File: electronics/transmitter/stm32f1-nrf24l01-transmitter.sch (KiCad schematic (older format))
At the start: 29 parts, among them K1 CONN_3, K10 CONN_3, K11 CONN_3, K2 CONN_3, K3 CONN_3, K4 CONN_3, K5 CONN_3, K6 CONN_3, K7 CONN_3, K8 CONN_3, K9 CONN_3, P1 Charge, P2 LED, P3 CONN_2, P4 CONN_2, P5 CONN_4, Q1 BC548, SW1 ON/OFF, U1 LIPO_CHARGER_+_PROTECTION, U2 STM32F103C8T6_DEV_BOARD, U3 NRF24L01P

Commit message: Update schematics
- Convert to KiCAD 4.05
- Dummy links accross battery connector for routing purpos
- Dummy connector for speaker
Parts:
- removed P5: CONN_4, symbol CONN_4
- added K12: CONN_3, Pin_Headers:Pin_Header_Straight_1x03_Pitch2.54mm, symbol CONN_3
- added P5: Buzzer, Pin_Headers:Pin_Header_Straight_1x02_Pitch2.54mm, symbol CONN_2
- BT1: footprint ~ -> (none)
- C1, C2: footprint ~ -> Capacitors_SMD:C_0805_HandSoldering; symbol C -> C-RESCUE-stm32f1-nrf24l01-transmitter
- K1, K10, K11, K2, K3, K4, K5, K6, K7, K8, K9: footprint (none) -> Pin_Headers:Pin_Header_Straight_1x03_Pitch2.54mm
- P1, P2, P3, P4: footprint (none) -> Pin_Headers:Pin_Header_Straight_1x02_Pitch2.54mm
- Q1: footprint ~ -> TO_SOT_Packages_THT:TO-92_Molded_Wide
- R1, R2, R3, R4: footprint ~ -> Resistors_SMD:R_0805_HandSoldering; symbol R -> R-RESCUE-stm32f1-nrf24l01-transmitter
- SP1: footprint ~ -> Buzzers_Beepers:Buzzer_12x9.5RM7.6
- SW1: footprint ~ -> Buttons_Switches_SMD:SW_SPST_FSMSM
- U1: footprint ~ -> WLA:LiPo_charger_and_protection
- U2: footprint ~ -> WLA:STM32F103C8T6
- U3: footprint ~ -> WLA:NRF24L01P-PA-LNA
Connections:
- wire segments 127 -> 131
- no-connect marks 5 -> 12
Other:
- note added: "Diagnostics UART"
- note removed: "Bluetooth SPP module\nDiagnostics UART"
- moved on the sheet: C1, C2, P2, Q1, SP1, U2, U3

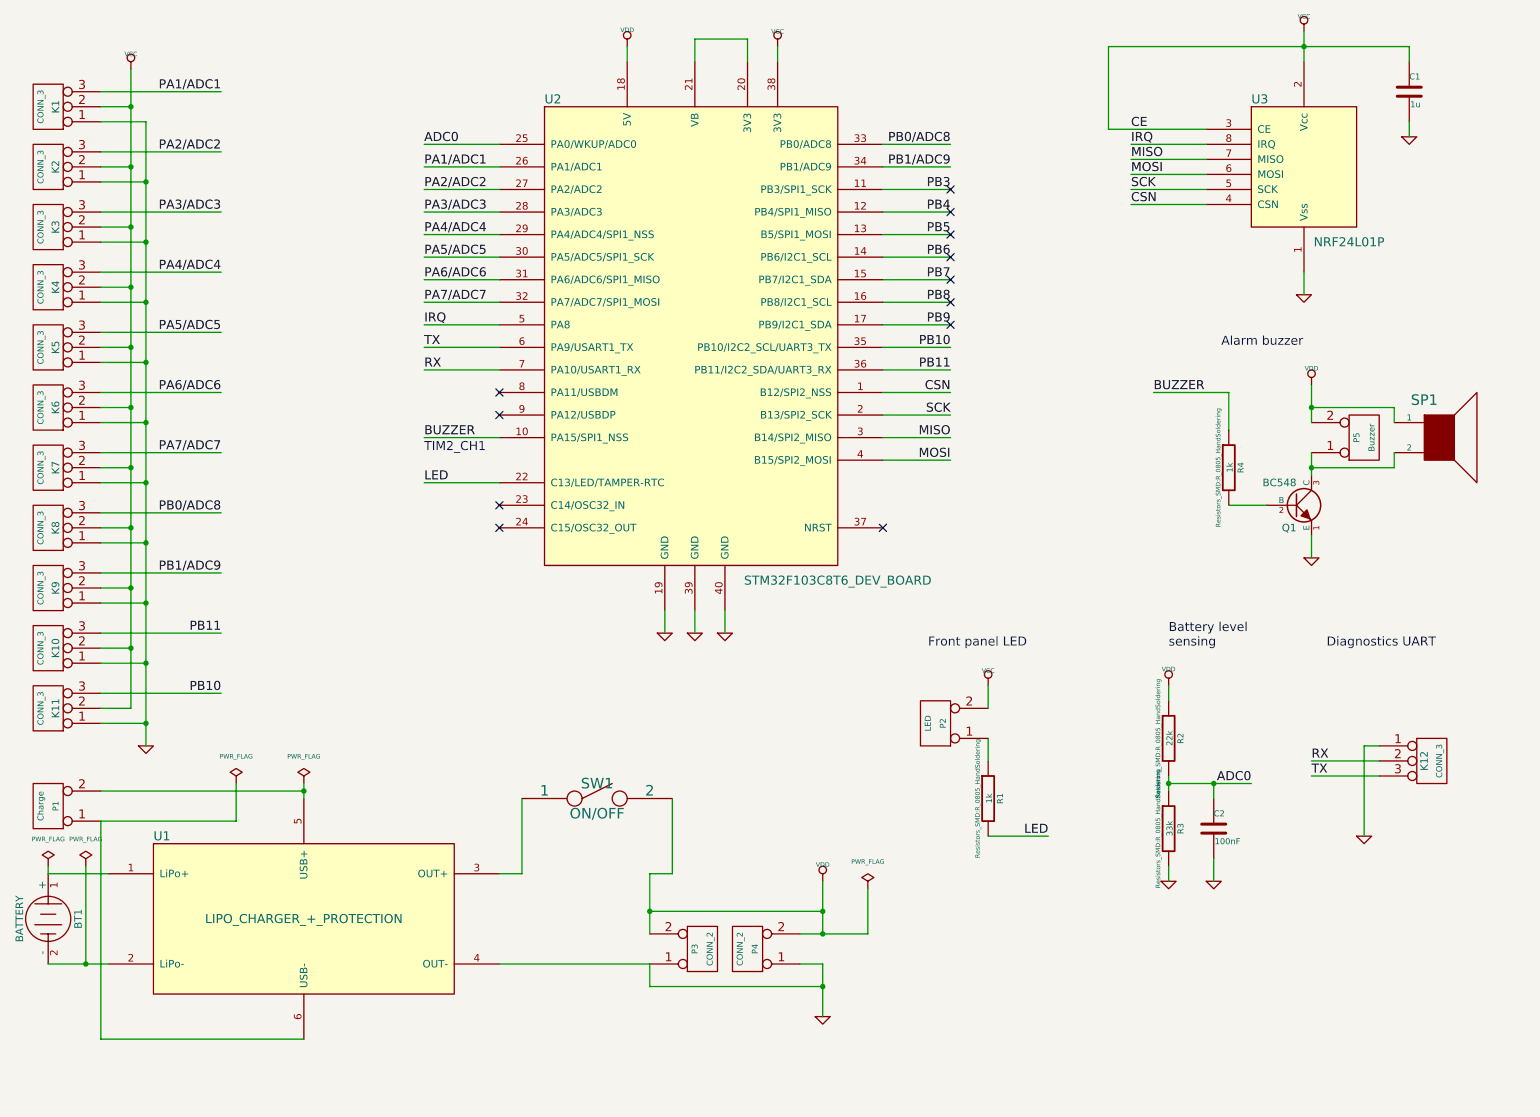
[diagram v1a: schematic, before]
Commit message: Tweak design to reduce space and wire links
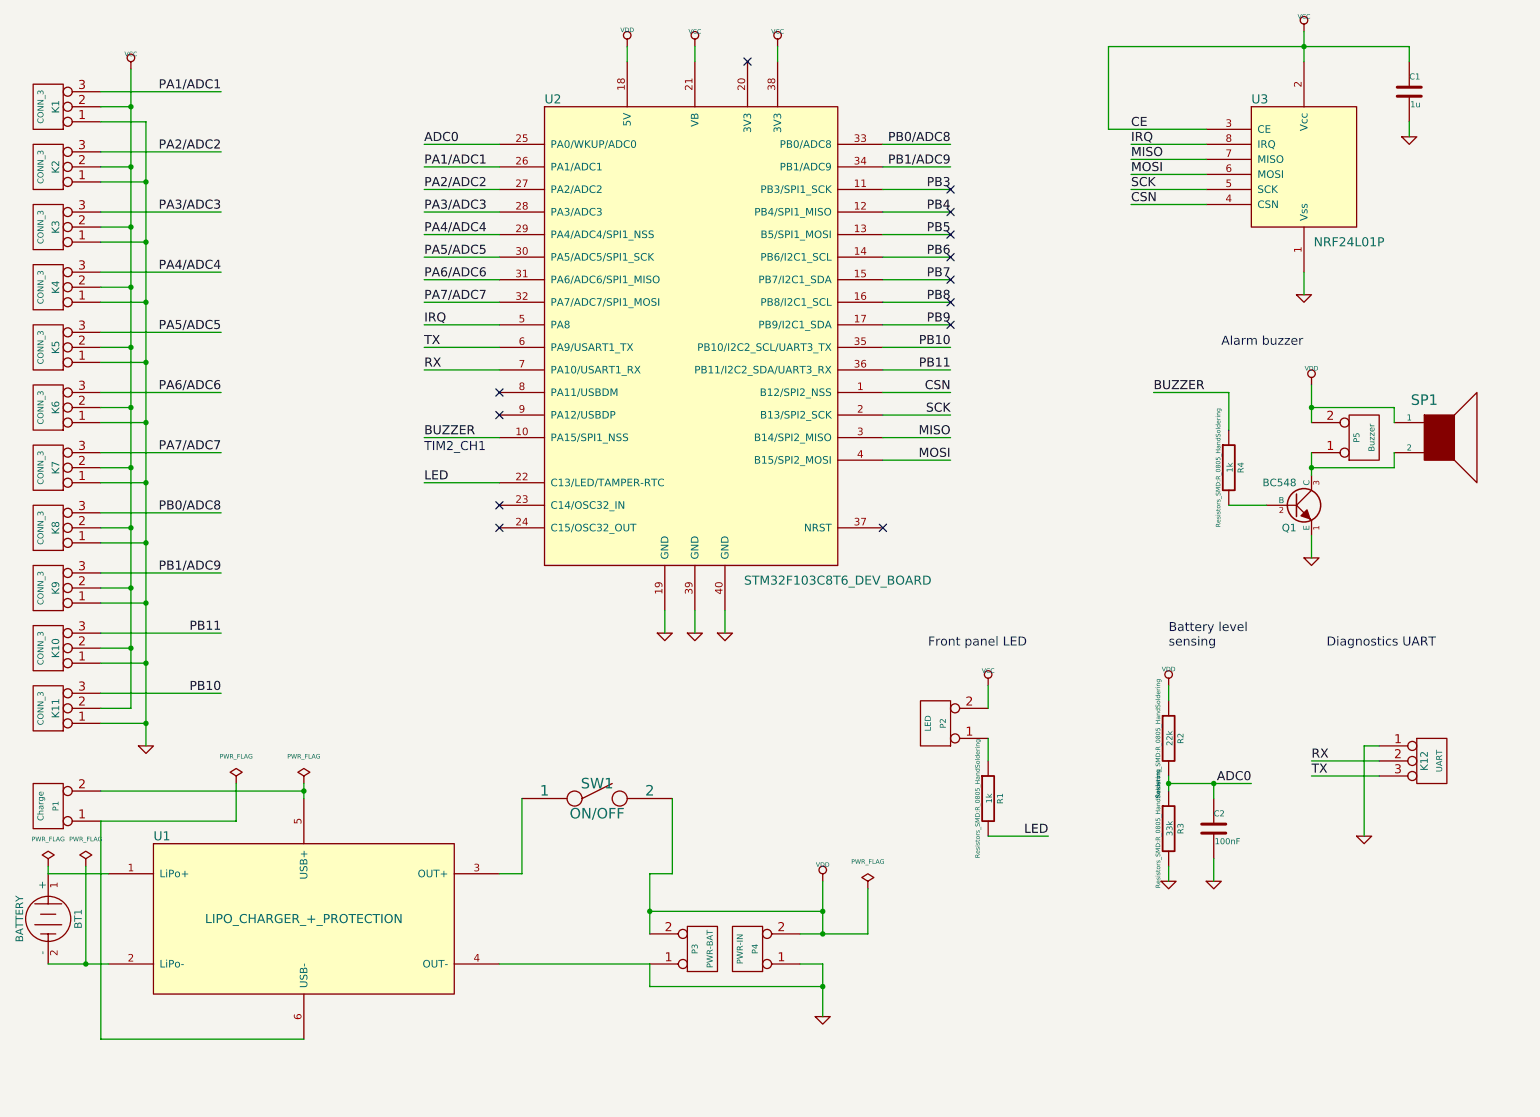
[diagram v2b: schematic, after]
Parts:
- K12: value CONN_3 -> UART
- P3: value CONN_2 -> PWR-BAT
- P4: value CONN_2 -> PWR-IN
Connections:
- net VCC: now also U2.21 (VB)
- net at U2.20 (3V3): no longer U2.21 (VB)
- no-connect marks 12 -> 13
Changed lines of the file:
@@
 P 5950 6850
 F 0 "P4" V 5900 6850 40  0000 C CNN
-F 1 "CONN_2" V 6000 6850 40  0000 C CNN
+F 1 "PWR-IN" V 6000 6850 40  0000 C CNN
 F 2 "Pin_Headers:Pin_Header_Straight_1x02_Pitch2.54mm" H 5950 6850 60  0001 C CNN
 F 3 "" H 5950 6850 60  0000 C CNN
@@
 P 5650 6850
 F 0 "P3" V 5600 6850 40  0000 C CNN
-F 1 "CONN_2" V 5700 6850 40  0000 C CNN
+F 1 "PWR-BAT" V 5700 6850 40  0000 C CNN
 F 2 "Pin_Headers:Pin_Header_Straight_1x02_Pitch2.54mm" H 5650 6850 60  0001 C CNN
 F 3 "" H 5650 6850 60  0000 C CNN
@@
 P 10500 5600
 F 0 "K12" V 10450 5600 50  0000 C CNN
-F 1 "CONN_3" V 10550 5600 40  0000 C CNN
+F 1 "UART" V 10550 5600 40  0000 C CNN
 F 2 "Pin_Headers:Pin_Header_Straight_1x03_Pitch2.54mm" H 10500 5600 60  0001 C CNN
 F 3 "" H 10500 5600 60  0000 C CNN
@@
 Wire Wire Line
 	6150 850  6150 950
-Wire Wire Line
-	5600 950  5600 800
-Wire Wire Line
-	5600 800  5950 800
-Wire Wire Line
-	5950 800  5950 950
 Wire Wire Line
 	8350 850  10350 850
@@
 NoConn ~ 7300 2550
 NoConn ~ 7300 2700
+$Comp
+L VCC #PWR?
+U 1 1 589BC63C
+P 5600 850
+F 0 "#PWR?" H 5600 950 30  0001 C CNN
+F 1 "VCC" H 5600 950 30  0000 C CNN
+F 2 "" H 5600 850 60  0000 C CNN
+F 3 "" H 5600 850 60  0000 C CNN
+	1    5600 850
+	1    0    0    -1
+$EndComp
+Wire Wire Line
+	5600 850  5600 950
+NoConn ~ 5950 950
 $EndSCHEMATC

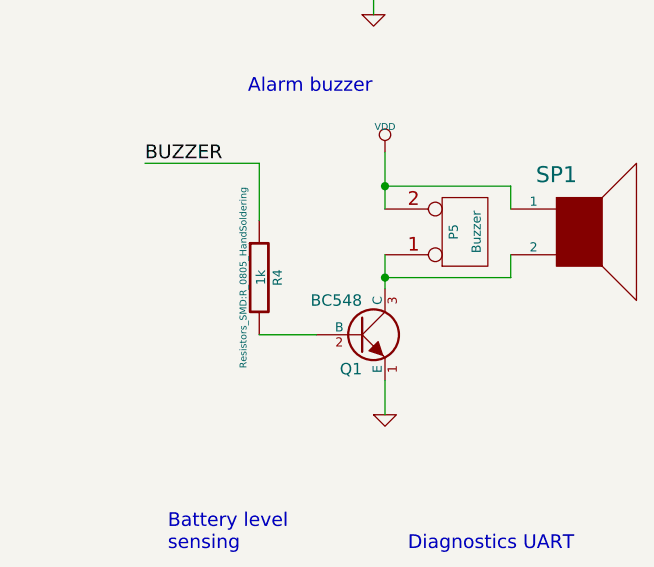
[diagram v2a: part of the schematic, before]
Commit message: Fix transistor footprint, add decoupling cap for buzzer, minor tweaks
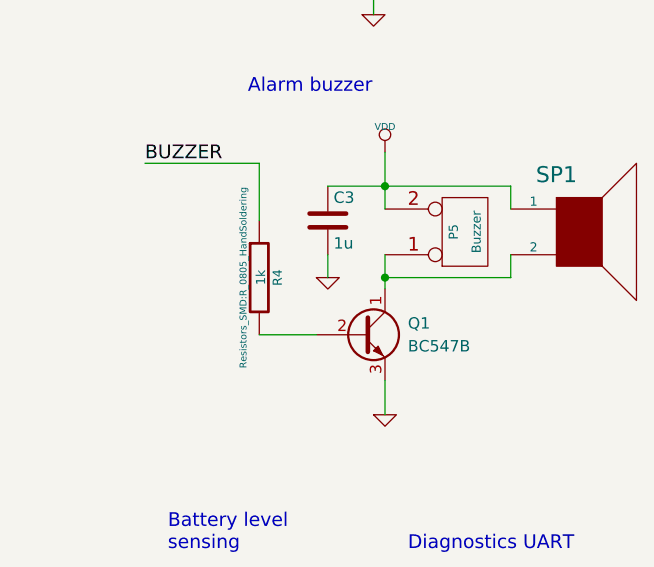
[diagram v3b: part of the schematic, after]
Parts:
- removed Q1: BC548, TO_SOT_Packages_THT:TO-92_Molded_Wide, symbol NPN
- added C3: 1u, Capacitors_SMD:C_0805_HandSoldering, symbol C
- added Q1: BC547B, TO_SOT_Packages_THT:TO-92_Inline_Wide, symbol Q_NPN_CBE
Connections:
- net GND: now also C3.2, Q1.3 (E)
- net VDD: now also C3.1
- net at P5.1 (P1), SP1.2: now also Q1.1 (C)
- net at R4.2: now also Q1.2 (B)
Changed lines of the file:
@@
-$EndComp
-$Comp
-L NPN Q1
-U 1 1 5720519E
-P 9600 3900
-F 0 "Q1" H 9600 3750 50  0000 R CNN
-F 1 "BC548" H 9600 4050 50  0000 R CNN
-F 2 "TO_SOT_Packages_THT:TO-92_Molded_Wide" H 9600 3900 60  0001 C CNN
-F 3 "~" H 9600 3900 60  0000 C CNN
-	1    9600 3900
-	1    0    0    -1
 $EndComp
 $Comp
@@
 Connection ~ 6450 7100
 Wire Wire Line
-	9700 3250 10250 3250
+	9450 3250 10250 3250
 Wire Wire Line
 	10250 3250 10250 3350
@@
 NoConn ~ 7300 2700
 $Comp
-L VCC #PWR?
+L VCC #PWR025
 U 1 1 589BC63C
 P 5600 850
-F 0 "#PWR?" H 5600 950 30  0001 C CNN
+F 0 "#PWR025" H 5600 950 30  0001 C CNN
 F 1 "VCC" H 5600 950 30  0000 C CNN
 F 2 "" H 5600 850 60  0000 C CNN
@@
 	5600 850  5600 950
 NoConn ~ 5950 950
+$Comp
+L Q_NPN_CBE Q1
+U 1 1 589EC521
+P 9600 3900
+F 0 "Q1" H 9800 3950 50  0000 L CNN
+F 1 "BC547B" H 9800 3850 50  0000 L CNN
+F 2 "TO_SOT_Packages_THT:TO-92_Inline_Wide" H 9800 4000 50  0001 C CNN
+F 3 "" H 9600 3900 50  0000 C CNN
+	1    9600 3900
+	1    0    0    -1
+$EndComp
+$Comp
+L C C3
+U 1 1 589ECC74
+P 9450 3400
+F 0 "C3" H 9475 3500 50  0000 L CNN
+F 1 "1u" H 9475 3300 50  0000 L CNN
+F 2 "Capacitors_SMD:C_0805_HandSoldering" H 9488 3250 50  0001 C CNN
+F 3 "" H 9450 3400 50  0000 C CNN
+	1    9450 3400
+	1    0    0    -1
+$EndComp
+$Comp
+L GND-RESCUE-stm32f1-nrf24l01-transmitter #PWR026
+U 1 1 589ECD1A
+P 9450 3650
+F 0 "#PWR026" H 9450 3650 30  0001 C CNN
+F 1 "GND" H 9450 3580 30  0001 C CNN
+F 2 "" H 9450 3650 60  0000 C CNN
+F 3 "" H 9450 3650 60  0000 C CNN
+	1    9450 3650
+	1    0    0    -1
+$EndComp
+Wire Wire Line
+	9450 3550 9450 3650
 $EndSCHEMATC

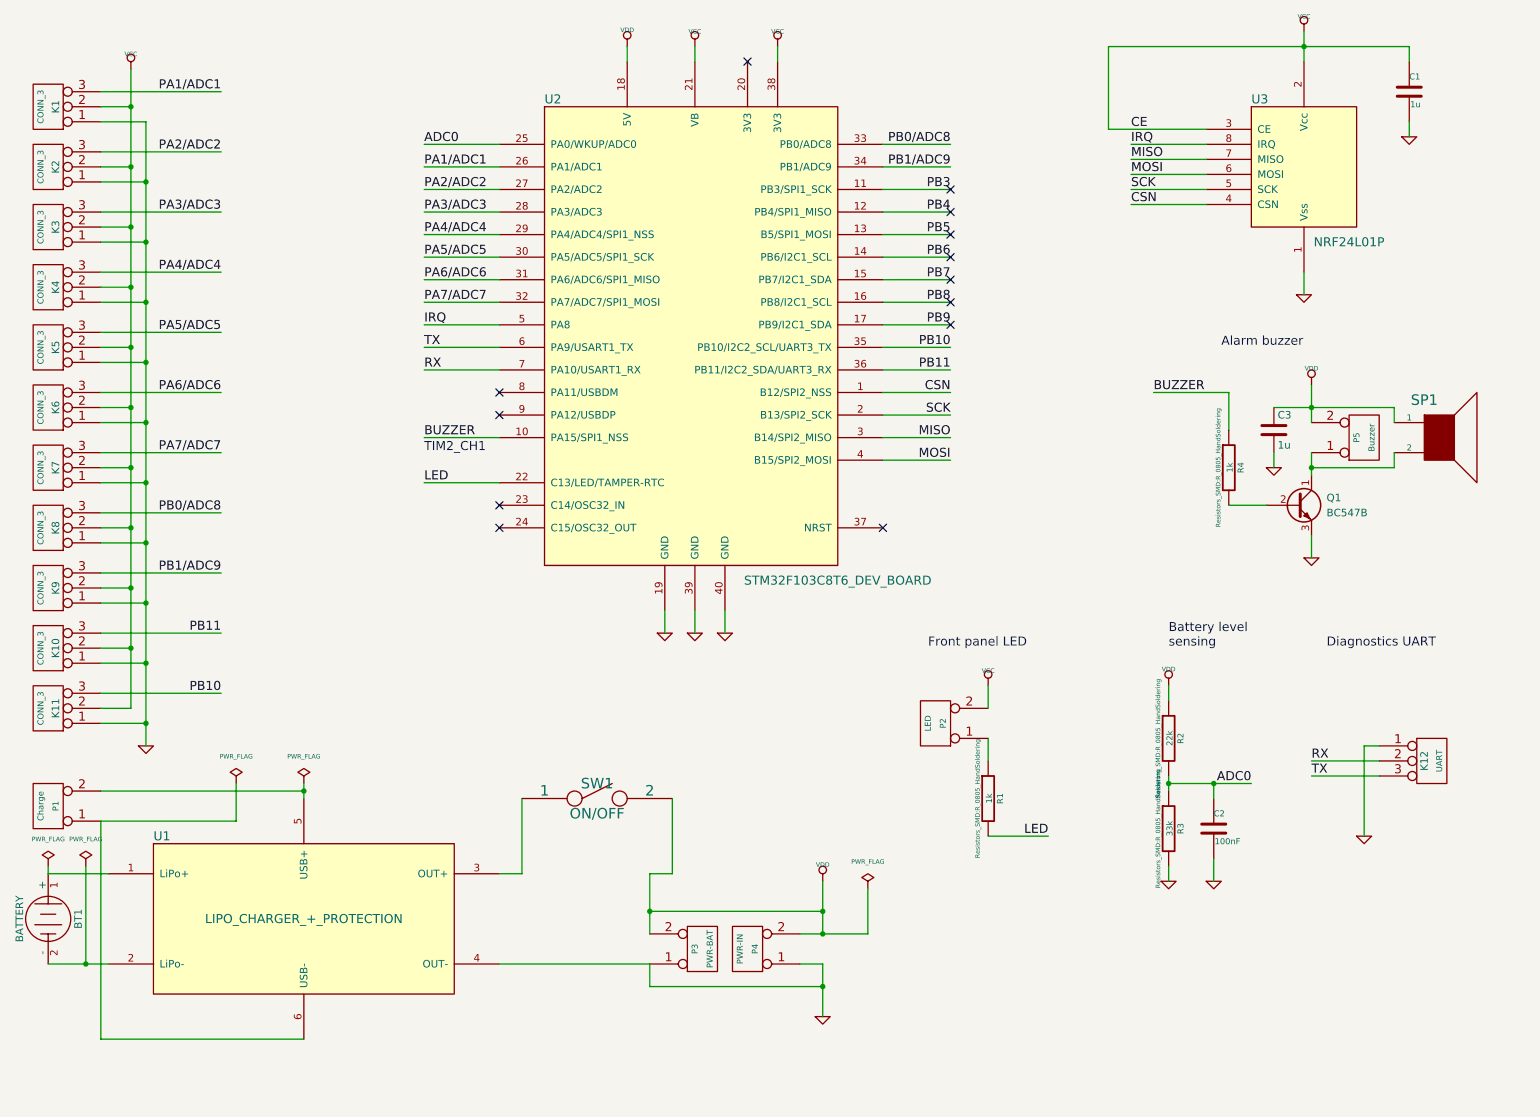
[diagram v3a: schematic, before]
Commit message: Add analog meter output to electronics
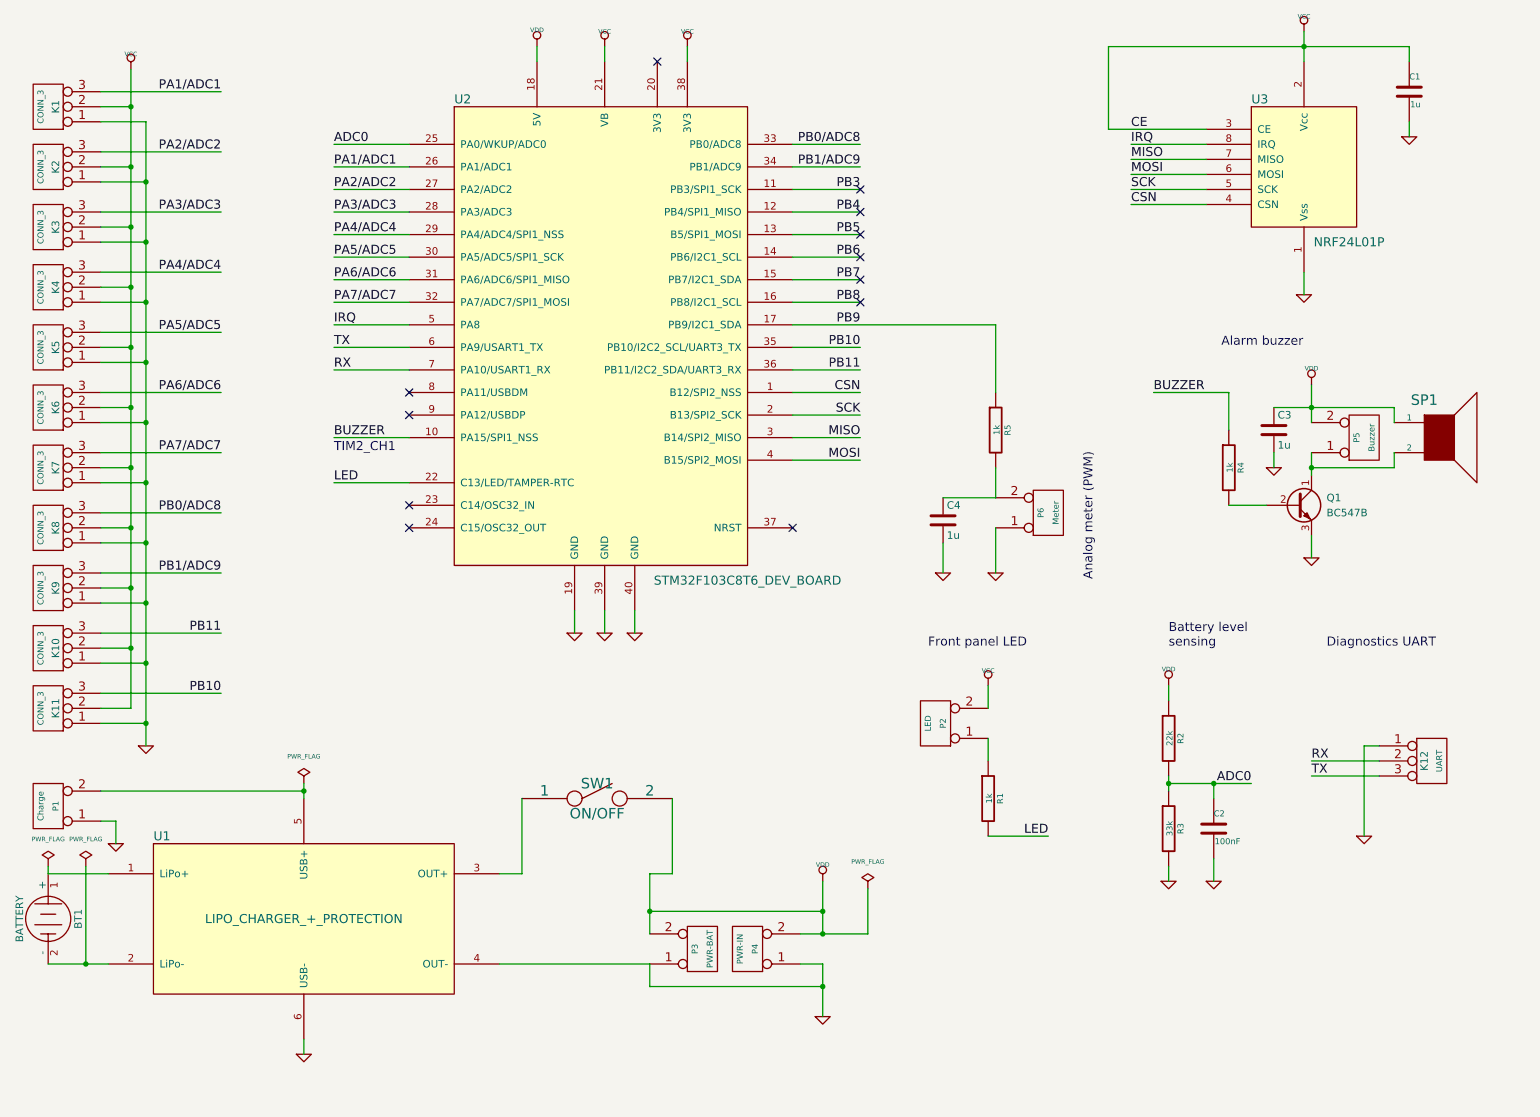
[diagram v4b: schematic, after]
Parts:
- added C4: 1u, Capacitors_SMD:C_0805_HandSoldering, symbol C
- added P6: Meter, Pin_Headers:Pin_Header_Straight_1x02_Pitch2.54mm, symbol CONN_2
- added R5: 1k, Resistors_SMD:R_0805_HandSoldering, symbol R-RESCUE-stm32f1-nrf24l01-transmitter
- BT1: footprint (none) -> Pin_Headers:Pin_Header_Straight_1x02_Pitch2.54mm
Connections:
- net GND: now also P1.1 (P1), U1.6 (USB-), C4.2, P6.1 (P1)
- net PB9: now also R5.1
- new net: C4.1, P6.2 (PM), R5.2
- no-connect marks 13 -> 12
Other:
- note added: "Analog meter (PWM)"
- moved on the sheet: U2

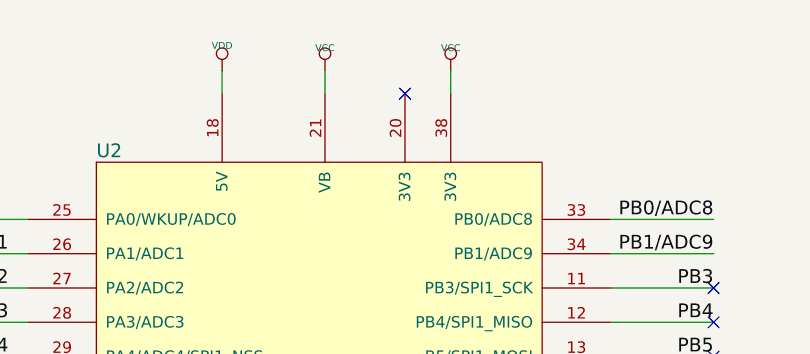
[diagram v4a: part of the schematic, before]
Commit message: Tweak Airtronics PCB design
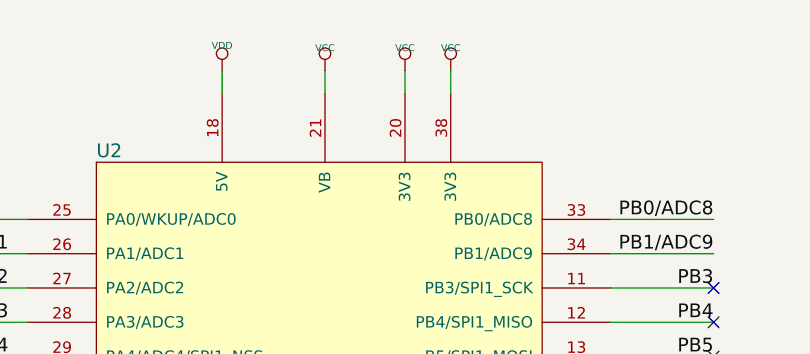
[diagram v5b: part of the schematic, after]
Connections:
- net VCC: now also U2.20 (3V3)
- no-connect marks 12 -> 11
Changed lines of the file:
@@
 Wire Wire Line
 	5000 850  5000 950
-NoConn ~ 5350 950
 $Comp
 L Q_NPN_CBE Q1
@@
 	1    0    0    -1
 $EndComp
+$Comp
+L VCC #PWR?
+U 1 1 58D2422E
+P 5350 850
+F 0 "#PWR?" H 5350 950 30  0001 C CNN
+F 1 "VCC" H 5350 950 30  0000 C CNN
+F 2 "" H 5350 850 60  0000 C CNN
+F 3 "" H 5350 850 60  0000 C CNN
+	1    5350 850
+	1    0    0    -1
+$EndComp
+Wire Wire Line
+	5350 850  5350 950
 $EndSCHEMATC
